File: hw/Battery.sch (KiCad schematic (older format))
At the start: 12 parts, among them Q1 AO3400, Q2 AO3400, U2 TP4056

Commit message: multiple changes
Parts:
- U2: symbol charger2-rescue:TP4056-TP4056 -> charger2-rescue:TP4056-TP4056-charger2-rescue
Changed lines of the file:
@@
 	7950 3100 7950 3200
 $Comp
-L charger2-rescue:TP4056-TP4056 U?
+L charger2-rescue:TP4056-TP4056-charger2-rescue U?
 U 1 1 5DD277B2
 P 5100 2700

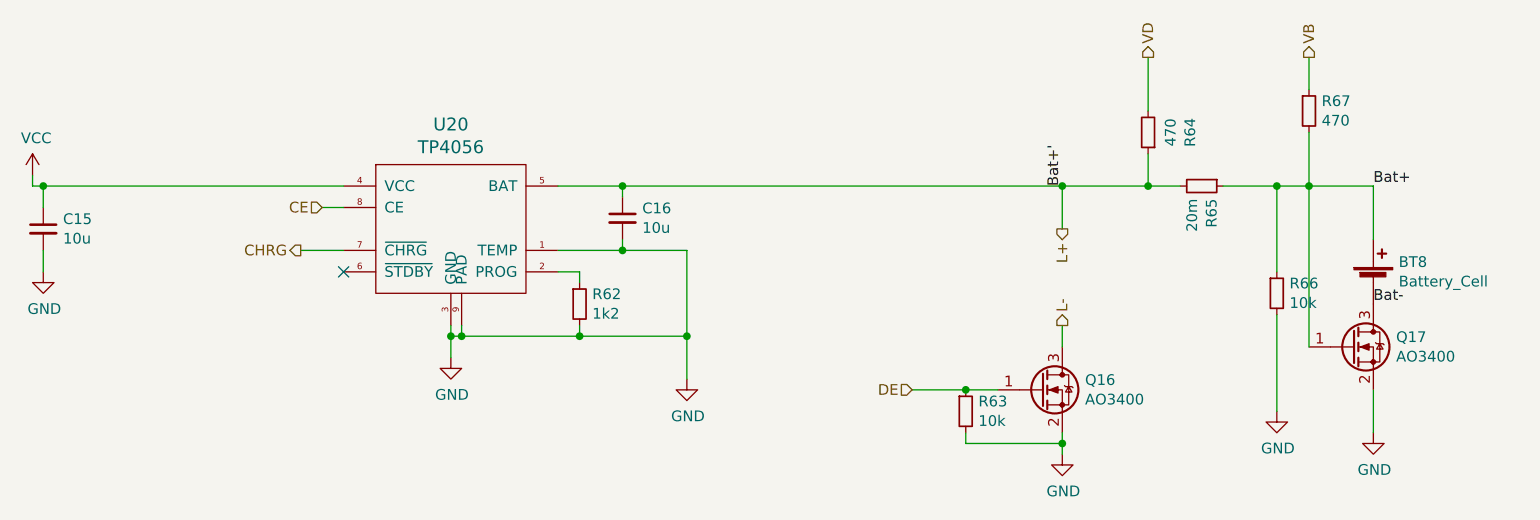
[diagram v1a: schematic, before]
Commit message: fix mux enable pin, reroute some traces
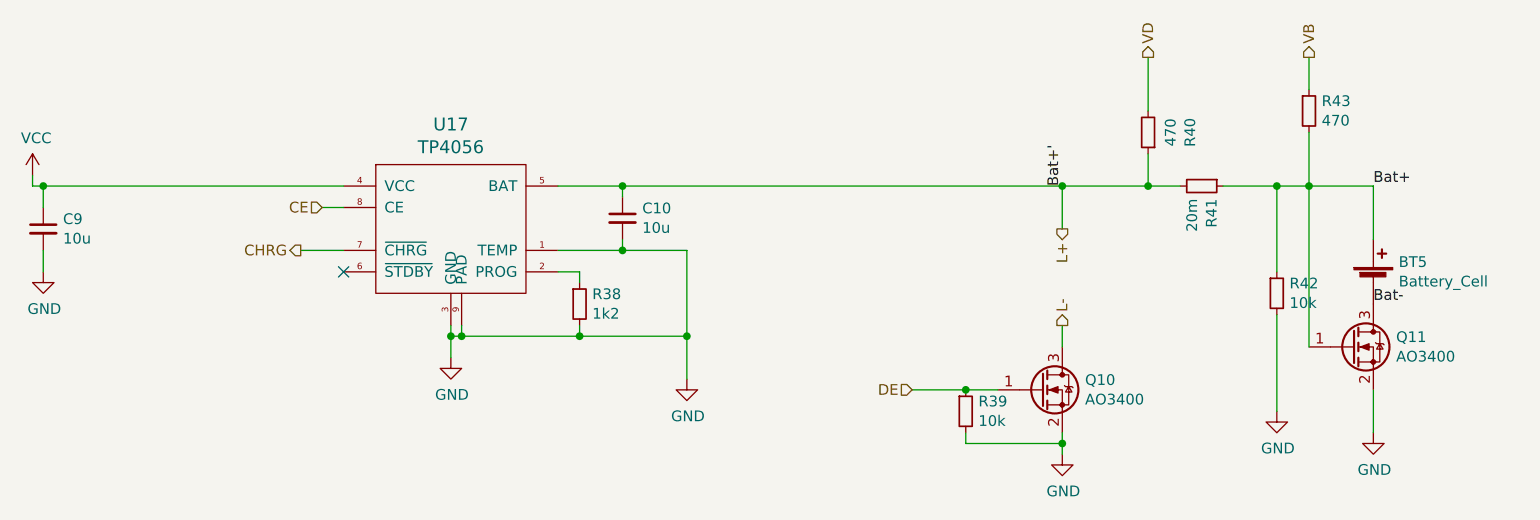
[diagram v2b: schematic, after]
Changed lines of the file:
@@
 EESchema Schematic File Version 4
-LIBS:charger2-cache
 EELAYER 30 0
 EELAYER END
@@
 AR Path="/5DE37049/5DC5D9F3/5DC7184E" Ref="R?"  Part="1"
 AR Path="/5DE37049/5DC5DB65/5DC7184E" Ref="R?"  Part="1"
-F 0 "R62" H 5759 3046 50  0000 L CNN
+F 0 "R38" H 5759 3046 50  0000 L CNN
 F 1 "1k2" H 5759 2955 50  0000 L CNN
 F 2 "Resistor_SMD:R_0805_2012Metric_Pad1.15x1.40mm_HandSolder" H 5700 3000 50  0001 C CNN
@@
 AR Path="/5DE37049/5DC5D9F3/5DD277C3" Ref="Q?"  Part="1"
 AR Path="/5DE37049/5DC5DB65/5DD277C3" Ref="Q?"  Part="1"
-F 0 "Q17" H 9506 3246 50  0000 L CNN
+F 0 "Q11" H 9506 3246 50  0000 L CNN
 F 1 "AO3400" H 9506 3155 50  0000 L CNN
 F 2 "Package_TO_SOT_SMD:SOT-23_Handsoldering" H 9500 3300 50  0001 C CNN
@@
 AR Path="/5DE37049/5DC5D9F3/5DD277B6" Ref="R?"  Part="1"
 AR Path="/5DE37049/5DC5DB65/5DD277B6" Ref="R?"  Part="1"
-F 0 "R63" H 7559 3546 50  0000 L CNN
+F 0 "R39" H 7559 3546 50  0000 L CNN
 F 1 "10k" H 7559 3455 50  0000 L CNN
 F 2 "Resistor_SMD:R_0805_2012Metric_Pad1.15x1.40mm_HandSolder" H 7500 3500 50  0001 C CNN
@@
 AR Path="/5DE37049/5DC5D9F3/5DD277B8" Ref="R?"  Part="1"
 AR Path="/5DE37049/5DC5DB65/5DD277B8" Ref="R?"  Part="1"
-F 0 "R67" H 9159 2146 50  0000 L CNN
+F 0 "R43" H 9159 2146 50  0000 L CNN
 F 1 "470" H 9159 2055 50  0000 L CNN
 F 2 "Resistor_SMD:R_0805_2012Metric_Pad1.15x1.40mm_HandSolder" H 9100 2100 50  0001 C CNN
@@
 AR Path="/5DE37049/5DC5D9F3/5DD277B9" Ref="C?"  Part="1"
 AR Path="/5DE37049/5DC5DB65/5DD277B9" Ref="C?"  Part="1"
-F 0 "C16" H 5992 2646 50  0000 L CNN
+F 0 "C10" H 5992 2646 50  0000 L CNN
 F 1 "10u" H 5992 2555 50  0000 L CNN
 F 2 "Capacitor_SMD:C_0805_2012Metric_Pad1.15x1.40mm_HandSolder" H 5900 2600 50  0001 C CNN
@@
 AR Path="/5DE37049/5DC5D9F3/5DD277BA" Ref="C?"  Part="1"
 AR Path="/5DE37049/5DC5DB65/5DD277BA" Ref="C?"  Part="1"
-F 0 "C15" H 3292 2696 50  0000 L CNN
+F 0 "C9" H 3292 2696 50  0000 L CNN
 F 1 "10u" H 3292 2605 50  0000 L CNN
 F 2 "Capacitor_SMD:C_0805_2012Metric_Pad1.15x1.40mm_HandSolder" H 3200 2650 50  0001 C CNN
@@
 AR Path="/5DE37049/5DC5D9F3/5DC4807B" Ref="R?"  Part="1"
 AR Path="/5DE37049/5DC5DB65/5DC4807B" Ref="R?"  Part="1"
-F 0 "R66" H 9009 2996 50  0000 L CNN
+F 0 "R42" H 9009 2996 50  0000 L CNN
 F 1 "10k" H 9009 2905 50  0000 L CNN
 F 2 "Resistor_SMD:R_0805_2012Metric_Pad1.15x1.40mm_HandSolder" H 8950 2950 50  0001 C CNN
@@
 AR Path="/5DE37049/5DC5D9F3/5DD277C1" Ref="BT?"  Part="1"
 AR Path="/5DE37049/5DC5DB65/5DD277C1" Ref="BT?"  Part="1"
-F 0 "BT8" H 9518 2996 50  0000 L CNN
+F 0 "BT5" H 9518 2996 50  0000 L CNN
 F 1 "Battery_Cell" H 9518 2905 50  0000 L CNN
 F 2 "Connector_PinSocket_2.54mm:PinSocket_1x02_P2.54mm_Vertical" V 9400 2960 50  0001 C CNN
@@
 AR Path="/5DE37049/5DC5D9F3/5DC270F2" Ref="R?"  Part="1"
 AR Path="/5DE37049/5DC5DB65/5DC270F2" Ref="R?"  Part="1"
-F 0 "R64" V 8154 2200 50  0000 C CNN
+F 0 "R40" V 8154 2200 50  0000 C CNN
 F 1 "470" V 8245 2200 50  0000 C CNN
 F 2 "Resistor_SMD:R_0805_2012Metric_Pad1.15x1.40mm_HandSolder" H 8350 2200 50  0001 C CNN
@@
 AR Path="/5DE37049/5DC5D9F3/5DC209D5" Ref="Q?"  Part="1"
 AR Path="/5DE37049/5DC5DB65/5DC209D5" Ref="Q?"  Part="1"
-F 0 "Q16" H 8056 3446 50  0000 L CNN
+F 0 "Q10" H 8056 3446 50  0000 L CNN
 F 1 "AO3400" H 8056 3355 50  0000 L CNN
 F 2 "Package_TO_SOT_SMD:SOT-23_Handsoldering" H 8050 3500 50  0001 C CNN
@@
 AR Path="/5DE37049/5DC5D9F3/5E1D2F9B" Ref="R?"  Part="1"
 AR Path="/5DE37049/5DC5DB65/5E1D2F9B" Ref="R?"  Part="1"
-F 0 "R65" H 8659 2496 50  0000 L CNN
+F 0 "R41" H 8659 2496 50  0000 L CNN
 F 1 "20m" H 8659 2405 50  0000 L CNN
 F 2 "Resistor_SMD:R_1206_3216Metric_Pad1.42x1.75mm_HandSolder" H 8600 2450 50  0001 C CNN
@@
 AR Path="/5DE37049/5DC5D9F3/5DD277B2" Ref="U?"  Part="1"
 AR Path="/5DE37049/5DC5DB65/5DD277B2" Ref="U?"  Part="1"
-F 0 "U20" H 5100 3237 60  0000 C CNN
+F 0 "U17" H 5100 3237 60  0000 C CNN
 F 1 "TP4056" H 5100 3131 60  0000 C CNN
 F 2 "Package_SO:SOP-8-1EP_4.57x4.57mm_P1.27mm_EP4.57x4.45mm_ThermalVias" H 5100 2700 60  0001 C CNN
